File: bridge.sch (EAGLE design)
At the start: 2 parts, among them P1 HEADERS23-2, P2 HEADERS23-2

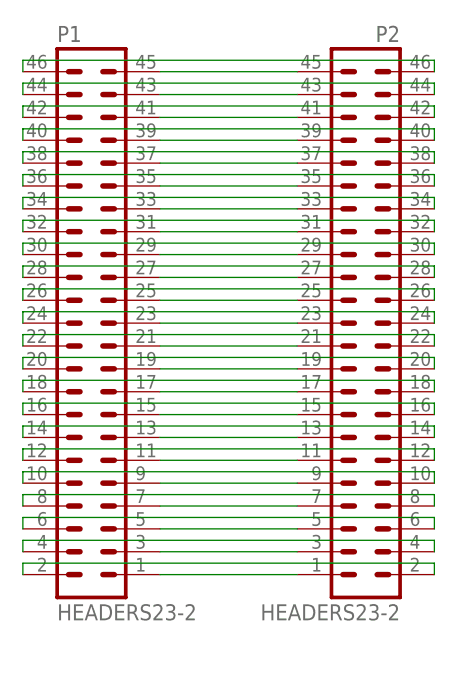
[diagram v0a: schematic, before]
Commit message: Add ground plane to bridge
This creates nice 50 Ohm impedance transmission lines (ish).
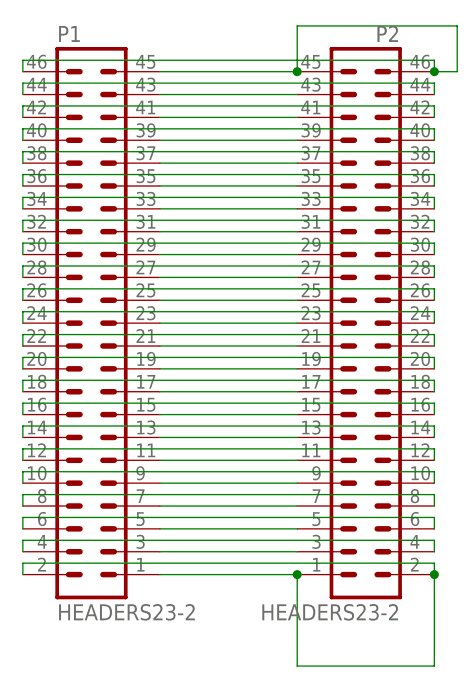
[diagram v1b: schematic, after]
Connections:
- removed net N$1: P1.1, P2.1
- removed net N$23: P1.45, P2.45
- removed net N$24: P1.2, P2.2
- removed net N$46: P1.46, P2.46
- new net GND: P1.1, P1.2, P1.45, P1.46, P2.1, P2.2, P2.45, P2.46
